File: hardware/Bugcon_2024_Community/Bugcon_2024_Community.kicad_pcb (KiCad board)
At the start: 2 copper layers, 99.7 x 86.6 mm, 38 parts, among them J2 Add_On, J3 OLED, J4 Battery, J5 Battery, P1 USB_C_Plug_USB2.0, Q1 DMG3415U-7, SW1 ON, U1 ESP32-C6-WROOM-1U-N4, U2 AP2112K-3.3

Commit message: feat(Hw): Update community PCB
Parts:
- removed the Ref** at (123.1, 82.6)
- added Ref**: Val**, Library:02.BugCON Personajes, F.Cu at (123.0, 82.6)
- moved J4 17.3 mm to (96.9, 113.3)
- moved J5 17.3 mm to (148.4, 96.0)
- moved R3 1.27 mm to (144.1, 75.8), turned to -53.5 degrees
- moved R6 1.06 mm to (86.5, 88.5), turned to 65 degrees
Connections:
- J2 pad 5: /GPIO3 -> unconnected-(J2-Pin_5-Pad5)
- J2 pad 6: /GPIO2 -> unconnected-(J2-Pin_6-Pad6)
- U1 pad 26: /GPIO3 -> /LED2
- U1 pad 27: /GPIO2 -> /LED1
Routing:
- net /VOUT: track 0.00 -> 174.4 mm, vias 0 -> 6
- net /RIGHT: track 0.00 -> 105.1 mm, vias 0 -> 3
- net /DOWN: track 0.00 -> 100.8 mm, vias 0 -> 1
- net /SDA: track 0.00 -> 93.3 mm, vias 0 -> 5
- net /SCL: track 0.00 -> 90.5 mm, vias 0 -> 5
- net /LED2: track 0.00 -> 80.1 mm, vias 0 -> 2
- net /EN: track 0.00 -> 79.9 mm, vias 0 -> 2
- net /LEFT: track 0.00 -> 76.2 mm, vias 0 -> 3
- net /UP: track 0.00 -> 43.3 mm, vias 0 -> 3
- net /BOOT: track 0.00 -> 41.8 mm
- net /D-: track 0.00 -> 40.7 mm
- net /D+: track 0.00 -> 40.7 mm
- net VBUS: track 0.00 -> 36.6 mm
- net /LED1: track 0.00 -> 17.3 mm
- net Net-(J4-Pin_1): track 0.00 -> 17.3 mm
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- added copper zone on B.Cu, net GND
- added copper zone on F.Cu, net GND

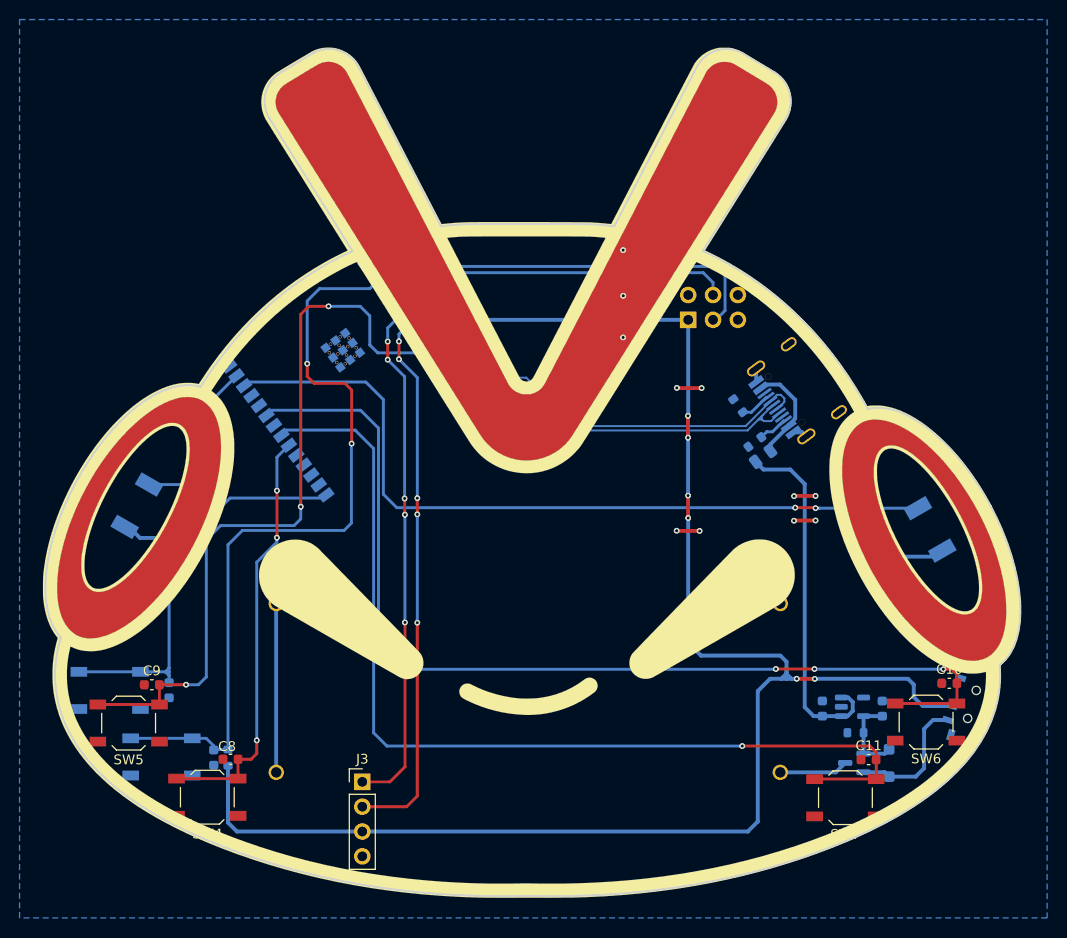
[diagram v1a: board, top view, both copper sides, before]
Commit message: feat(Hw): Update community route
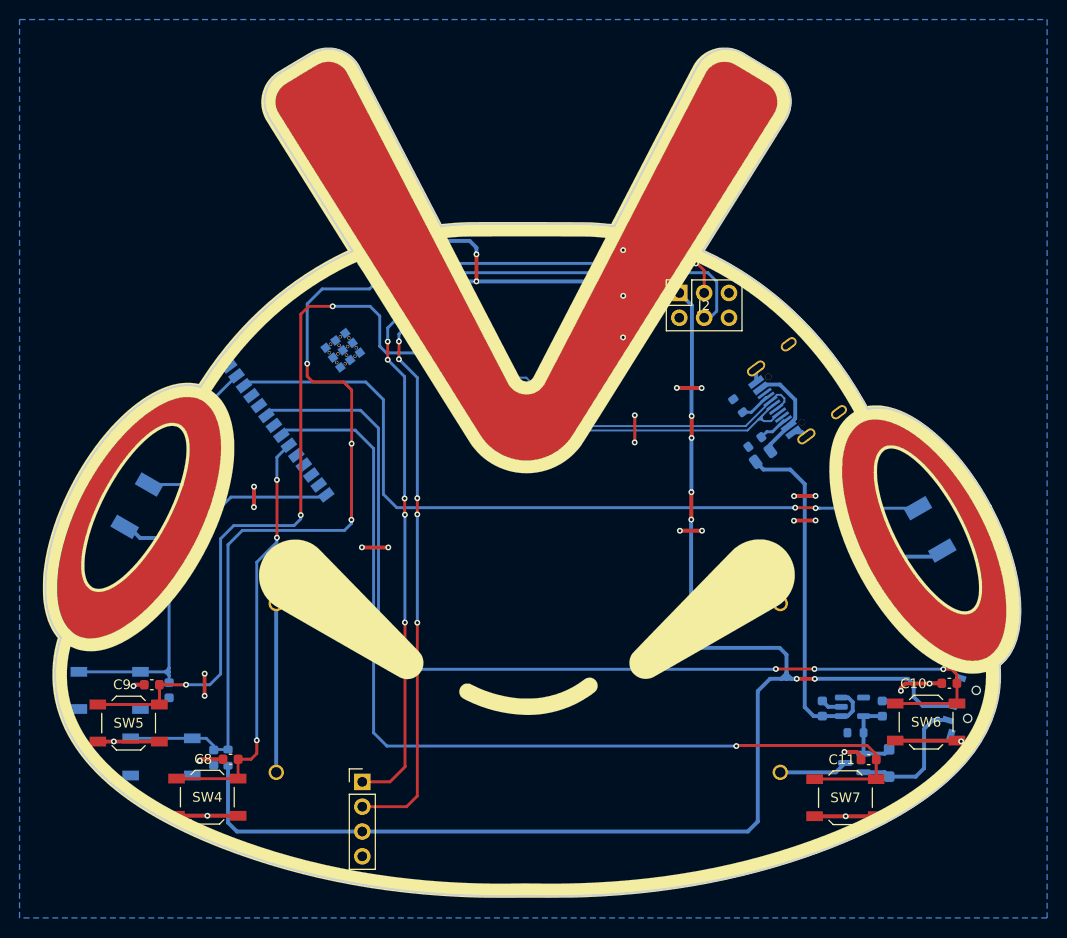
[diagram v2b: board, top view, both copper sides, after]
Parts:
- J2: moved to F.Cu
- moved J2 2.90 mm to (138.1, 64.2), turned to 90 degrees
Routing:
- net GND: track 12.2 -> 60.8 mm, vias 11 -> 28
- net /VOUT: track 174.4 -> 190.3 mm, vias 6 -> 8
- net /SDA: track 93.3 -> 88.3 mm, vias 5 -> 6
- net /SCL: track 90.5 -> 94.2 mm
- net /EN: track 79.9 -> 79.8 mm, vias 2 -> 3

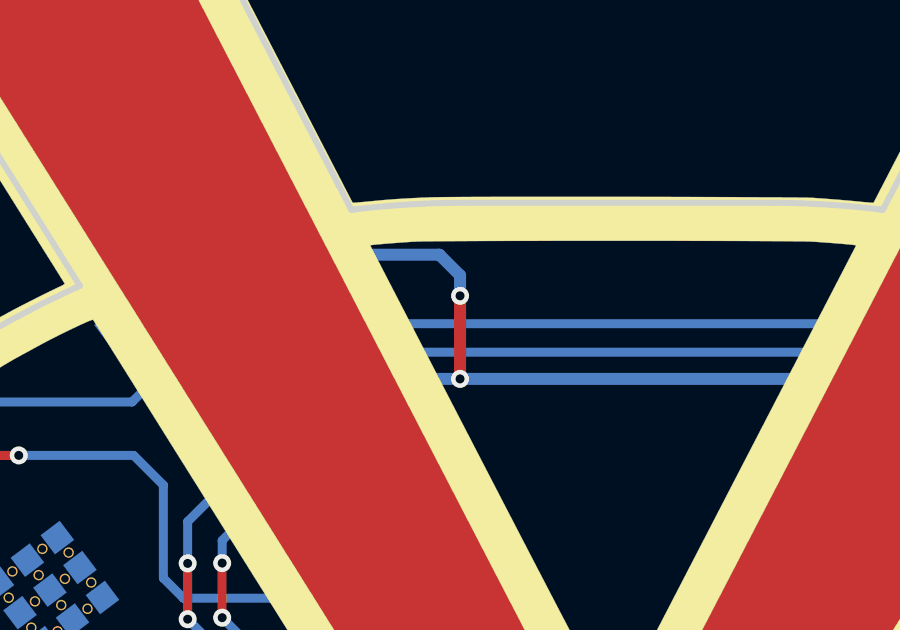
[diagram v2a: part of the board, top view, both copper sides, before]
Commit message: feat(Hw):Added_1A_Regulator
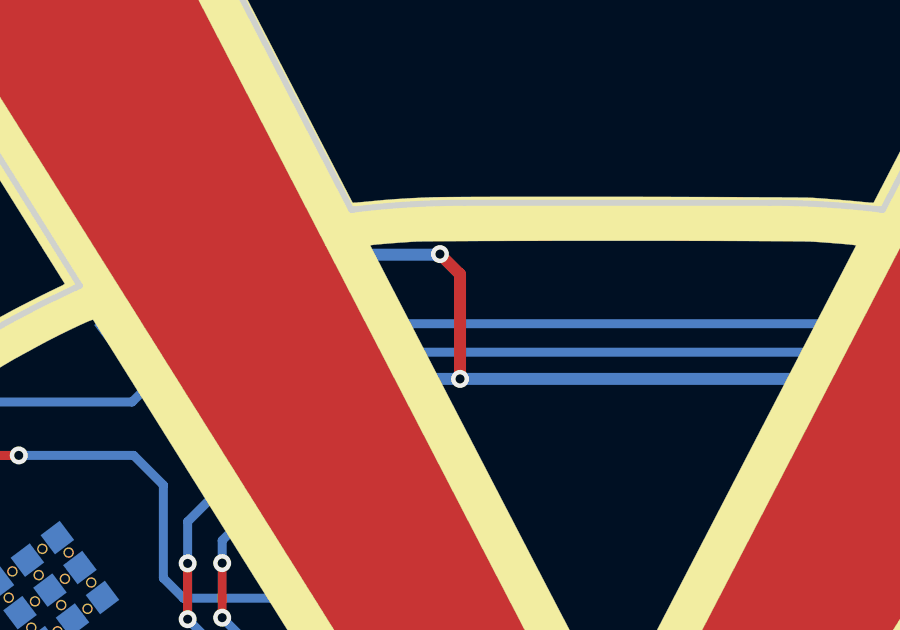
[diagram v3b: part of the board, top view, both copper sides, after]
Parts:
- U2: value AP2112K-3.3 -> XC6220B331MR-G
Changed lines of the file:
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@@
 		)
 		(fp_text user "${REFERENCE}"
-			(at -1.27 2.54 360)
+			(at -1.27 2.54 0)
 			(layer "F.Fab")
 			(effects
@@
 			)
 		)
-		(property "Value" "AP2112K-3.3"
+		(property "Value" "XC6220B331MR-G"
 			(at 0 -2.4 0)
 			(layer "B.Fab")
@@
 			)
 		)
-		(property "manf#" "AP2112K3.3TRG"
+		(property "manf#" "XC6220B331MR-G "
 			(at 0 0 180)
 			(unlocked yes)
@@
 			)
 		)
-		(property "LCSC#" "C51118"
+		(property "LCSC#" "C86534"
 			(at 0 0 180)
 			(unlocked yes)
@@
 		(fp_arc
 			(start -2.5 3.299998)
-			(mid -2.449999 3.250006)
+			(mid -2.449999 3.250007)
 			(end -2.399999 3.3)
 			(stroke
@@
 		(fp_arc
 			(start -2.5 3.299998)
-			(mid -2.449999 3.250006)
+			(mid -2.449999 3.250007)
 			(end -2.399999 3.3)
 			(stroke
@@
 	)
 	(segment
-		(start 117.36 63.05)
-		(end 117.36 60.28)
+		(start 116.688916 58.89)
+		(end 117.36 59.561084)
 		(width 0.4)
 		(layer "F.Cu")
@@
 		(net 4)
 	)
+	(segment
+		(start 117.36 59.561084)
+		(end 117.36 63.05)
+		(width 0.4)
+		(layer "F.Cu")
+		(net 4)
+	)
 	(via
 		(at 139.37 76.82)
@@
 	)
 	(via
-		(at 117.36 60.28)
+		(at 116.688916 58.89)
 		(size 0.6)
 		(drill 0.3)
@@
 	)
 	(segment
-		(start 116.669458 58.909458)
-		(end 111.050209 58.909458)
-		(width 0.4)
-		(layer "B.Cu")
-		(net 4)
-	)
-	(segment
 		(start 140.16 100.53)
 		(end 148.37 100.53)
@@
 	)
 	(segment
-		(start 117.36 60.28)
-		(end 117.36 59.6)
-		(width 0.4)
-		(layer "B.Cu")
-		(net 4)
-	)
-	(segment
-		(start 117.36 59.6)
+		(start 116.688916 58.89)
 		(end 116.669458 58.909458)
 		(width 0.4)
@@
 		(width 0.4)
 		(layer "B.Cu")
+		(net 4)
+	)
+	(segment
+		(start 116.669458 58.909458)
+		(end 111.050209 58.909458)
+		(width 0.4)
+		(layer "B.Cu")

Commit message: feat(Hw): Change LEDs
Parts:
- added R10: 330, Resistor_SMD:R_0603_1608Metric, B.Cu at (156.6, 86.4)
- added R11: 330, Resistor_SMD:R_0603_1608Metric, B.Cu at (159.0, 91.3)
- added R8: 330, Resistor_SMD:R_0603_1608Metric, B.Cu at (88.0, 84.2)
- added R9: 330, Resistor_SMD:R_0603_1608Metric, B.Cu at (156.6, 84.9)
- D2, D3: value Y_LED -> LED_RABG; footprint Library:LYT77K-K2M1 -> Library:AAA3528SURKCGKC09
- R6, R7: value 220 -> 330; footprint Resistor_SMD:R_0603_1608Metric_Pad0.98x0.95mm_HandSolder -> Resistor_SMD:R_0603_1608Metric
- moved R7 68.7 mm to (89.4, 84.8), turned to -110 degrees
- moved R6 9.26 mm to (77.8, 85.1), turned to -115 degrees
- moved D3 0.28 mm to (163.5, 88.4), turned to 118 degrees
- moved D2 0.17 mm to (82.7, 85.8), turned to -118 degrees
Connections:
- D2 pad 1: Net-(D2-K) -> Net-(D2-RK)
- D2 pad 2: /LED1 -> /VOUT
- D3 pad 1: Net-(D3-K) -> Net-(D3-RK)
- D3 pad 2: /LED2 -> /VOUT
- R6 pad 1: Net-(D2-K) -> /LED1
- R6 pad 2: GND -> Net-(D2-RK)
- R7 pad 1: Net-(D3-K) -> /LED2
- R7 pad 2: GND -> Net-(D2-GK)
- U1 pad 11: /PIN -> /LED5
- U1 pad 12: unconnected-(U1-IO11-Pad12) -> /LED4
- U1 pad 16: unconnected-(U1-IO18-Pad16) -> /LEFT
- U1 pad 19: unconnected-(U1-IO21-Pad19) -> /UP
- U1 pad 20: /UP -> /DOWN
- U1 pad 21: /DOWN -> /RIGHT
- U1 pad 23: /RIGHT -> /LED2
- U1 pad 26: /LED2 -> /LED3
- U1 pad 9: /LEFT -> /LED6
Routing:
- net /VOUT: track 190.4 -> 258.8 mm, vias 8 -> 12
- net /LED2: track 80.1 -> 12.1 mm, vias 2 -> 0
- net /LED6: track 0.00 -> 67.1 mm
- net /LED5: track 0.00 -> 56.9 mm
- net /LED4: track 0.00 -> 54.6 mm
- net /LEFT: track 76.2 -> 48.9 mm, vias 3 -> 1
- net /LED3: track 0.00 -> 13.2 mm
- net Net-(D2-GK): track 0.00 -> 8.20 mm
- net Net-(D3-K): track 6.55 -> 0.00 mm
- net Net-(D3-RK): track 0.00 -> 5.94 mm
- net Net-(D2-K): track 5.18 -> 0.00 mm
- net /LED1: track 17.3 -> 22.0 mm
- net Net-(D3-BK): track 0.00 -> 4.33 mm
- net Net-(D3-GK): track 0.00 -> 4.19 mm
- net Net-(D2-RK): track 0.00 -> 4.15 mm
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
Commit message: feat(Hw):Update_Route_And_Labels
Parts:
- added kibuzzard-666C89F7: G***, kibuzzard-666C89F7, B.Cu at (135.2, 66.8)
- added kibuzzard-666C89F7: G***, kibuzzard-666C89F7, B.Cu at (152.7, 96.0)
- added kibuzzard-666C8A00: G***, kibuzzard-666C8A00, B.Cu at (152.4, 113.3)
- added kibuzzard-66F475F7: G***, kibuzzard-66F475F7, B.Cu at (79.8, 101.0)
- added kibuzzard-66F47603: G***, kibuzzard-66F47603, B.Cu at (85.1, 115.5)
- added kibuzzard-66F4760F: G***, kibuzzard-66F4760F, F.Cu at (78.3, 104.5)
- added kibuzzard-66F4761D: G***, kibuzzard-66F4761D, F.Cu at (86.5, 111.9)
- added kibuzzard-66F4762A: G***, kibuzzard-66F4762A, F.Cu at (160.5, 104.2)
- added kibuzzard-66F47638: G***, kibuzzard-66F47638, F.Cu at (153.1, 112.0)
- added kibuzzard-66F47642: G***, kibuzzard-66F47642, B.Cu at (163.2, 107.1)
- added kibuzzard-66F47655: G***, kibuzzard-66F47655, B.Cu at (164.3, 102.7)
- added kibuzzard-66F47715: G***, kibuzzard-66F47715, B.Cu at (135.2, 64.2)

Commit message: feat(Hw):Added_Hole_And_Review
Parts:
- moved R1 1.73 mm to (115.6, 69.3), turned to -53 degrees
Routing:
- net GND: track 63.1 -> 73.5 mm
- net /EN: track 79.3 -> 80.5 mm
- net /VOUT: track 258.8 -> 259.8 mm
- net /UP: track 42.6 -> 41.8 mm
- net /SDA: vias 4 -> 2
- net /SCL: vias 3 -> 1
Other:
- outline, holes or cut-outs redrawn

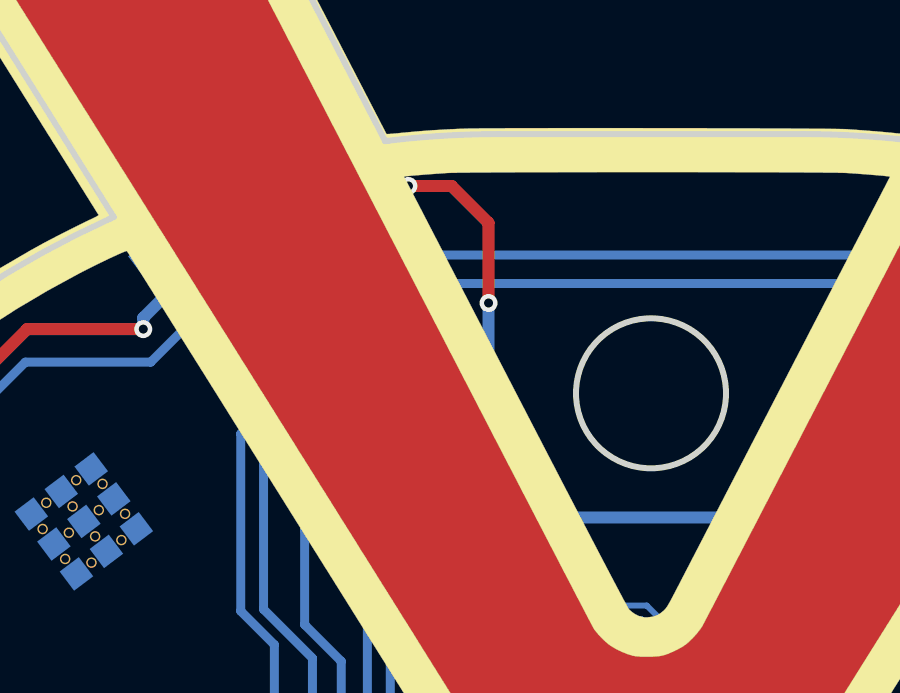
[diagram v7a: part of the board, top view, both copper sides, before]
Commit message: feat(Hw):Update_Labels
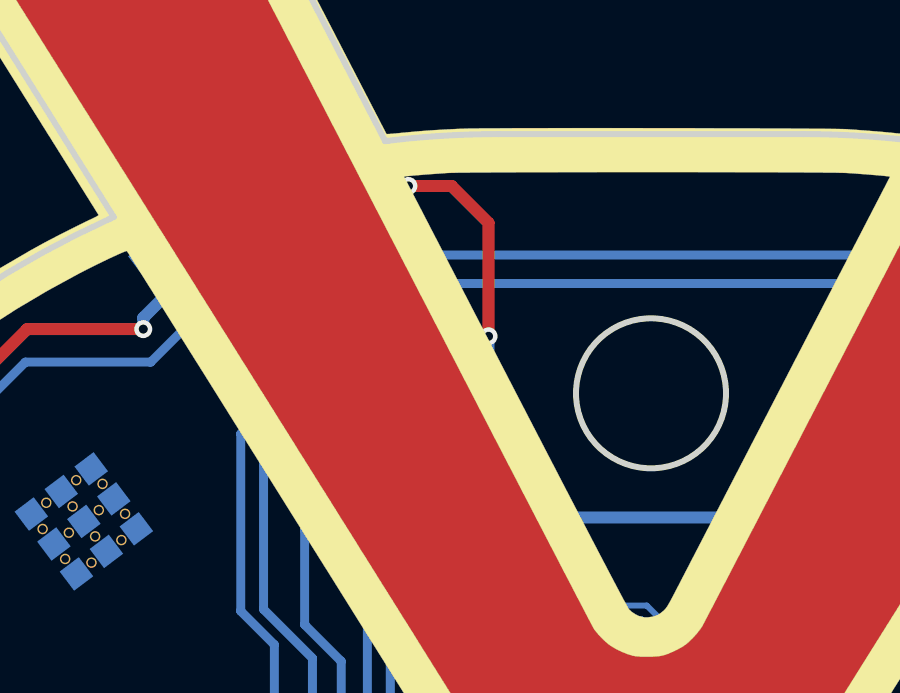
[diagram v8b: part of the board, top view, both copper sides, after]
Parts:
- added G***: LOGO, Aesthetics:electronic_cats_logo_8x6, B.Cu at (126.4, 79.0)
